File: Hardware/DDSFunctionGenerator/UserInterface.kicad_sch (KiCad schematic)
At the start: 9 parts, among them J7 Conn_01x04_Male, SW1 EN11-VSB1AQ15

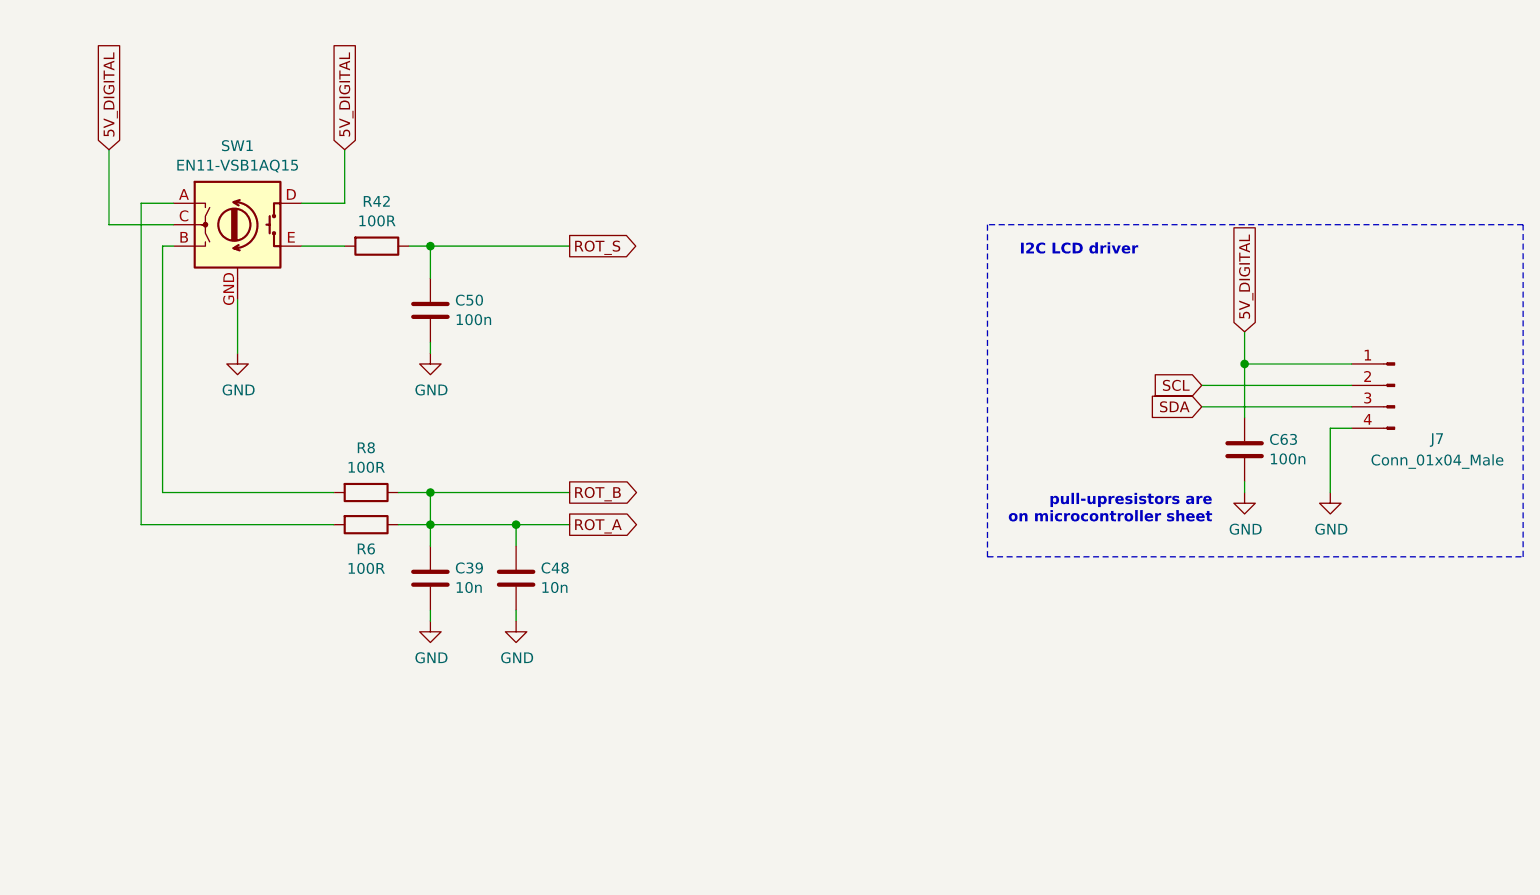
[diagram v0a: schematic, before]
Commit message: move to raspbbery pico, first draft
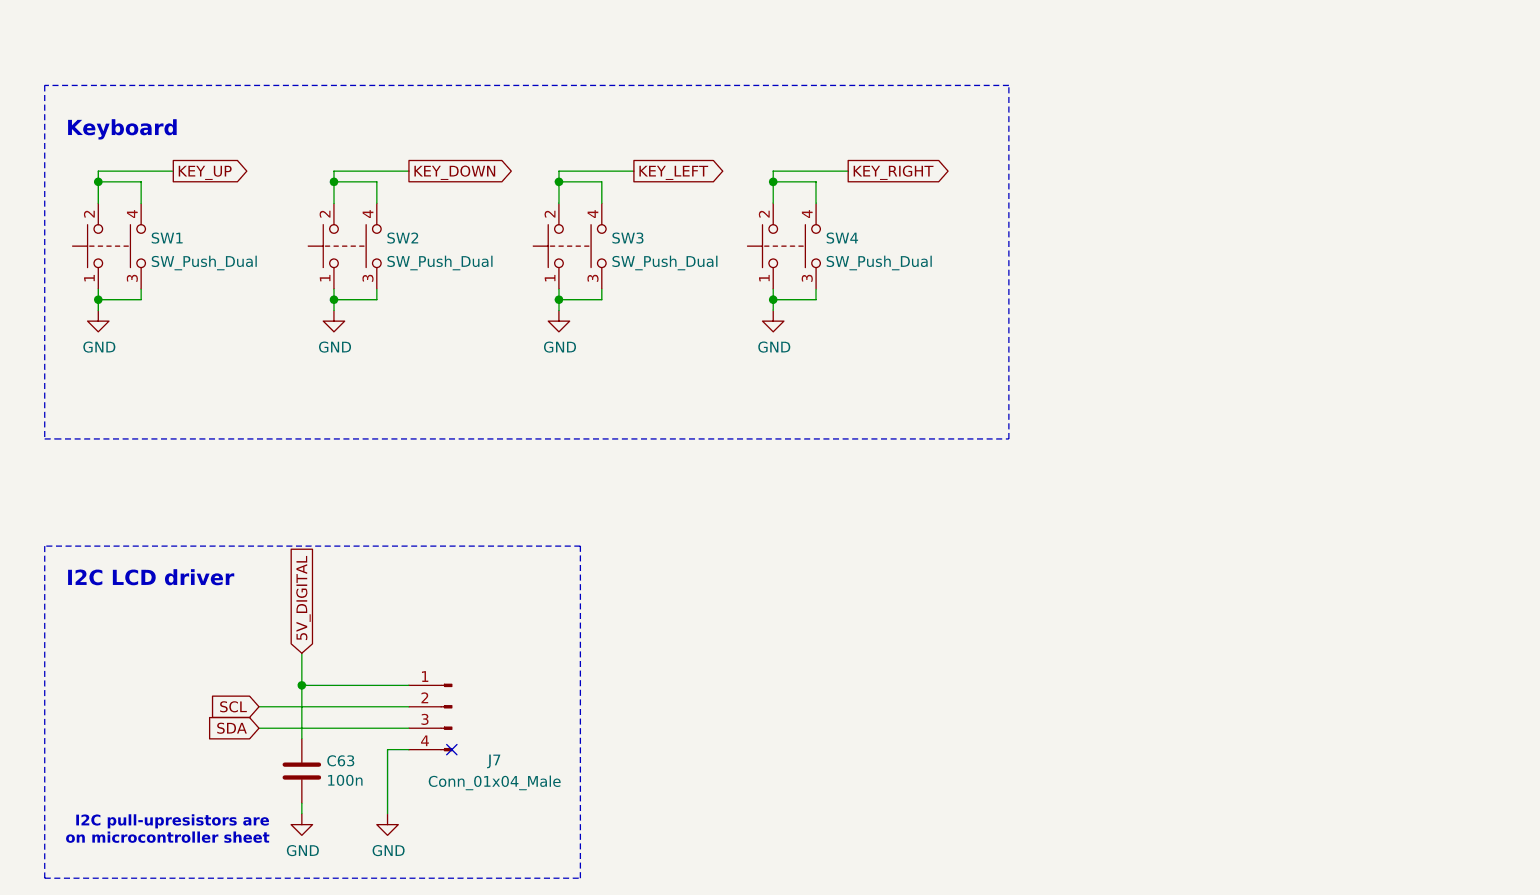
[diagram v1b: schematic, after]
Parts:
- removed C39, C48: 10n, Capacitor_SMD:C_0402_1005Metric, symbol Device:C
- removed C50: 100n, Capacitor_SMD:C_0402_1005Metric, symbol Device:C
- removed R42, R6, R8: 100R, Resistor_SMD:R_0402_1005Metric, symbol Device:R
- removed SW1: EN11-VSB1AQ15, DDSFunctionGenerator:EN11-VNB1BQ15, symbol NumericallyControlledOscillator:EN11-VSB1AQ15
- added SW1, SW2, SW3, SW4: SW_Push_Dual, symbol Switch:SW_Push_Dual
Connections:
- net GND: now also SW1.1, SW1.3, SW2.1, SW2.3, SW3.1, SW3.3, SW4.1, SW4.3
- new net KEY_DOWN: SW2.2, SW2.4
- new net KEY_LEFT: SW3.2, SW3.4
- new net KEY_RIGHT: SW4.2, SW4.4
- new net KEY_UP: SW1.2, SW1.4
- no-connect marks 0 -> 1
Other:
- note added: "I2C pull-upresistors are on microcontroller sheet"
- note added: "Keyboard"
- note removed: "pull-upresistors are on microcontroller sheet"
- moved on the sheet: C63, J7
